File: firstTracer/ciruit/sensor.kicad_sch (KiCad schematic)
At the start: 16 parts, among them Q3 MMBT3906, Q4 MMBT3906, U2 NJL5901AR, U3 NJL5901AR

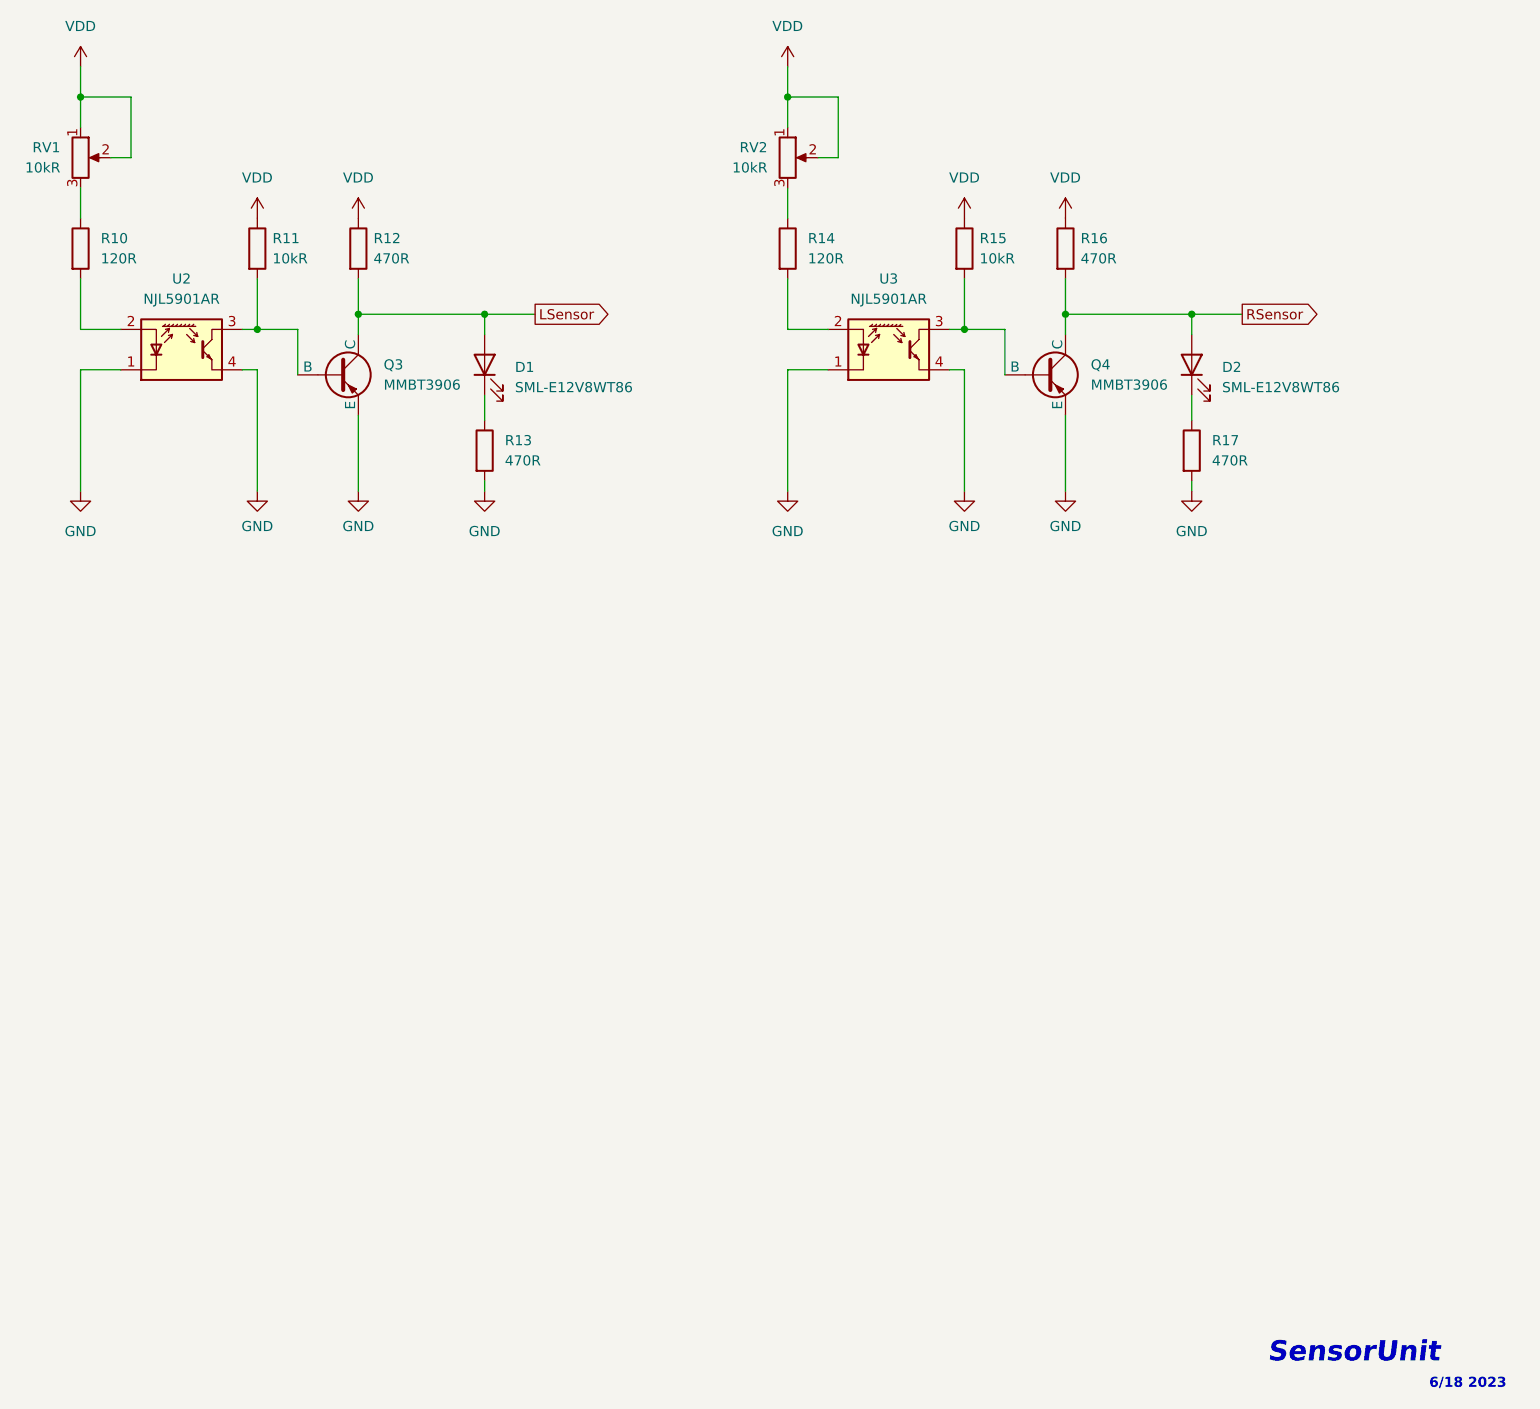
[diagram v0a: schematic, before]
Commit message: jikken2: fix circuit
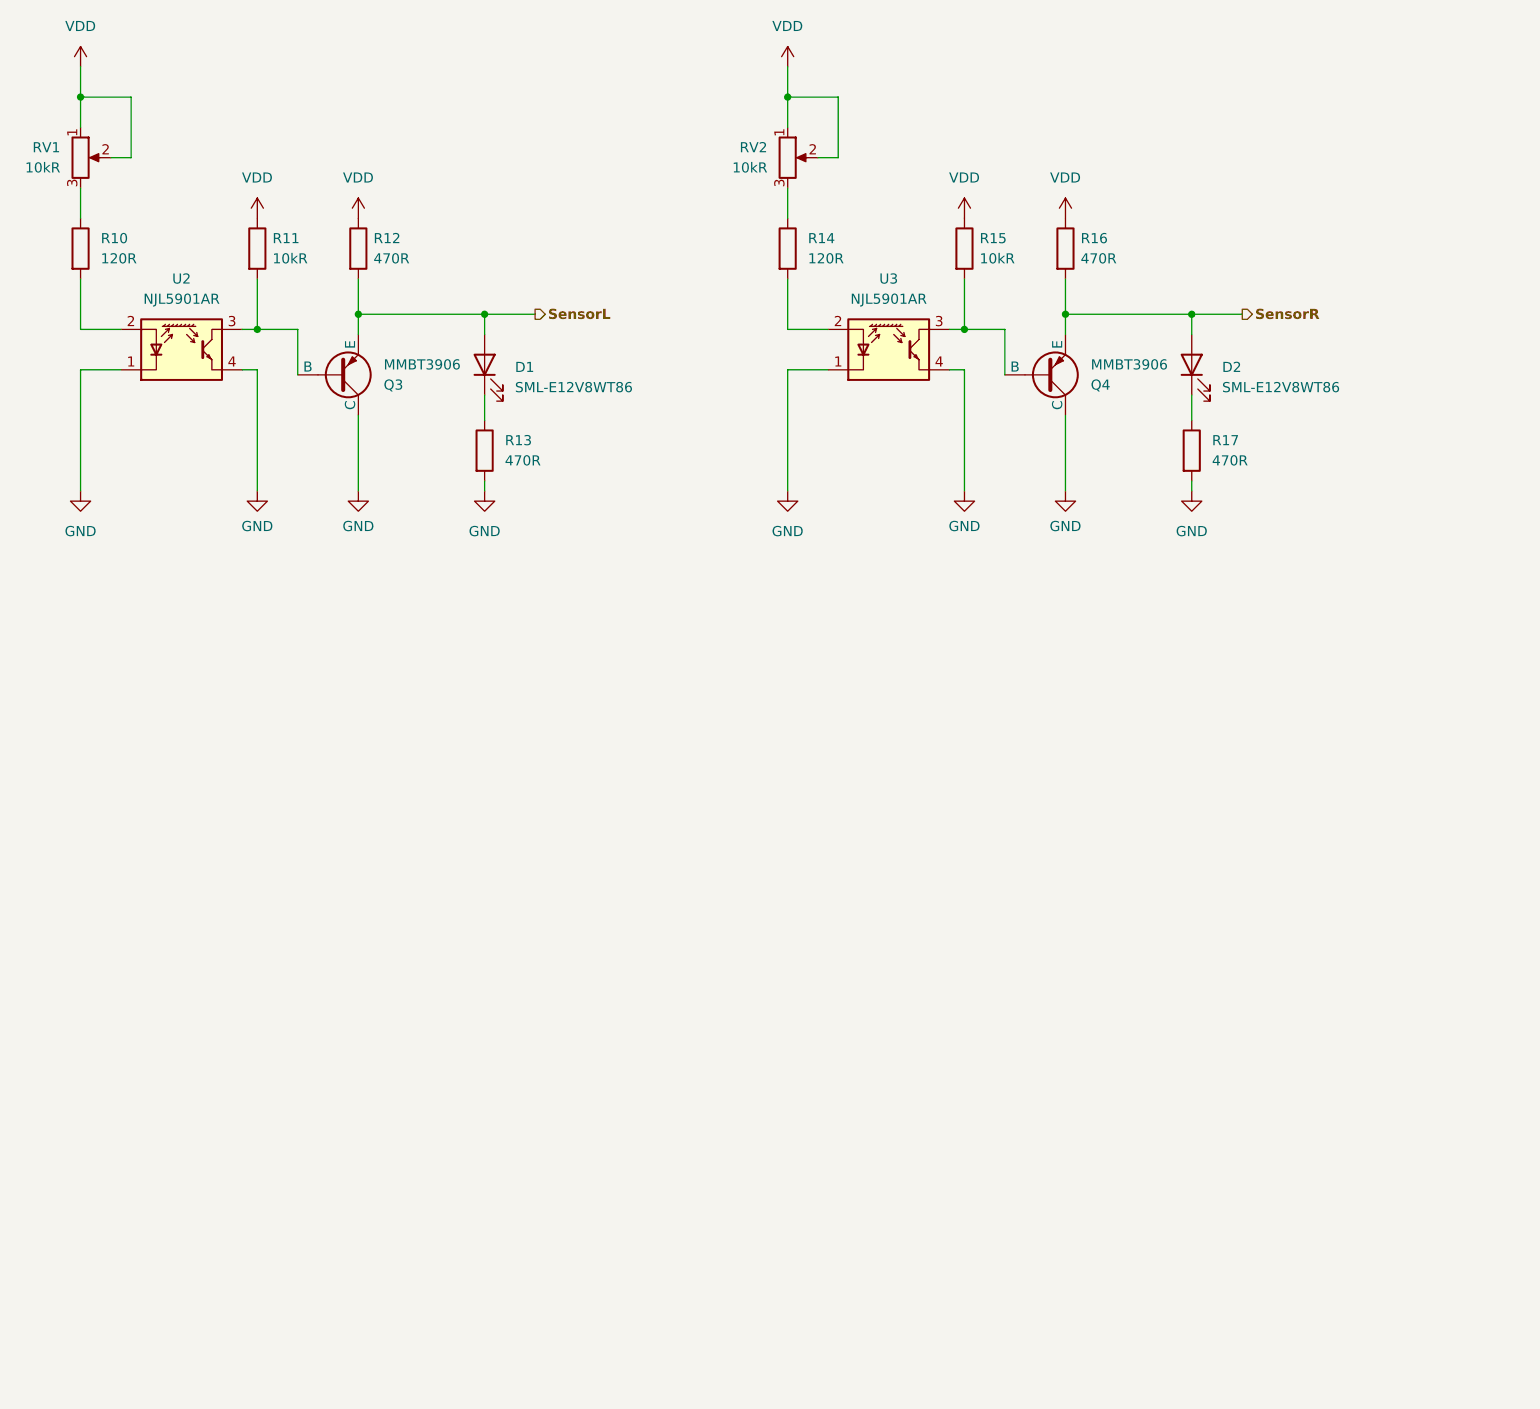
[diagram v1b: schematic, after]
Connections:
- net GND: now also Q3.1 (C), Q4.1 (C); no longer Q3.3 (E), Q4.3 (E)
- net LSensor renamed SensorL
- net SensorL: now also Q3.3 (E); no longer Q3.1 (C)
- net RSensor renamed SensorR
- net SensorR: now also Q4.3 (E); no longer Q4.1 (C)
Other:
- note removed: "6/18 2023"
- note removed: "SensorUnit"
- company: (none) -> KCCTD4-8
- title: (none) -> LineTracer-Practice-Sensor
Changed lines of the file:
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@@
 (kicad_sch (version 20230121) (generator eeschema)
   (paper "A4")
+  (title_block
+    (title "LineTracer-Practice-Sensor")
+    (date "2023-06-18")
+    (rev "BETA")
+    (company "KCCTD4-8")
+    (comment 1 "*Unless otherwise noted, resistors used are 1/4W resistors.")
+    (comment 2 ">>>UNCHECKED CIRCUIT<<<")
+  )
   (junction (at 88.9 59.055) (diameter 0) (color 0 0 0 0)
   )
@@
     (stroke (width 0) (type default))
   )
-  (text "6/18 2023" (at 207.645 194.31 0)
-    (effects (font (size 1.27 1.27) bold) (justify left bottom))
-  )
-  (text "SensorUnit" (at 187.325 191.135 0)
-    (effects (font (size 2.54 2.54) (thickness 0.508) bold italic) (justify left bottom))
-  )
-  (global_label "RSensor" (shape output) (at 184.15 59.055 0) (fields_autoplaced)
-    (effects (font (size 1.27 1.27)) (justify left))
-    (property "Intersheetrefs" "${INTERSHEET_REFS}" (at 194.7362 59.055 0)
-      (effects (font (size 1.27 1.27)) (justify left) hide)
-    )
-  )
-  (global_label "LSensor" (shape output) (at 95.25 59.055 0) (fields_autoplaced)
-    (effects (font (size 1.27 1.27)) (justify left))
-    (property "Intersheetrefs" "${INTERSHEET_REFS}" (at 105.5943 59.055 0)
-      (effects (font (size 1.27 1.27)) (justify left) hide)
-    )
+  (hierarchical_label "SensorL" (shape output) (at 95.25 59.055 0) (fields_autoplaced)
+    (effects (font (size 1.27 1.27) bold) (justify left))
+  )
+  (hierarchical_label "SensorR" (shape output) (at 184.15 59.055 0) (fields_autoplaced)
+    (effects (font (size 1.27 1.27) bold) (justify left))
   )
   (symbol (lib_id "Device:R_Potentiometer") (at 127 39.37 0) (unit 1)
@@
     )
   )
-  (symbol (lib_id "Simulation_SPICE:PNP") (at 70.485 66.675 0) (unit 1)
-    (in_bom yes) (on_board yes) (dnp no) (fields_autoplaced)
-    (property "Reference" "Q3" (at 76.2 65.405 0)
-      (effects (font (size 1.27 1.27)) (justify left))
-    )
-    (property "Value" "MMBT3906" (at 76.2 67.945 0)
+  (symbol (lib_id "Simulation_SPICE:PNP") (at 70.485 66.675 0) (mirror x) (unit 1)
+    (in_bom yes) (on_board yes) (dnp no)
+    (property "Reference" "Q3" (at 76.2 67.945 0)
+      (effects (font (size 1.27 1.27)) (justify left))
+    )
+    (property "Value" "MMBT3906" (at 76.2 65.405 0)
       (effects (font (size 1.27 1.27)) (justify left))
     )
@@
     )
   )
-  (symbol (lib_id "Simulation_SPICE:PNP") (at 159.385 66.675 0) (unit 1)
-    (in_bom yes) (on_board yes) (dnp no) (fields_autoplaced)
-    (property "Reference" "Q4" (at 165.1 65.405 0)
-      (effects (font (size 1.27 1.27)) (justify left))
-    )
-    (property "Value" "MMBT3906" (at 165.1 67.945 0)
-      (effects (font (size 1.27 1.27)) (justify left))
-    )
+  (symbol (lib_id "Simulation_SPICE:PNP") (at 159.385 66.675 0) (mirror x) (unit 1)
+    (in_bom yes) (on_board yes) (dnp no)
+    (property "Reference" "Q4" (at 165.1 67.945 0)
+      (effects (font (size 1.27 1.27)) (justify left))
+    )
+    (property "Value" "MMBT3906" (at 165.1 65.405 0)
+      (effects (font (size 1.27 1.27)) (justify left))
+    )
